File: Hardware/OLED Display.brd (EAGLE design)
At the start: 44.4 x 12.7 mm, 34 parts, among them J1 QWIIC_RIGHT_ANGLE, J3 QWIIC_RIGHT_ANGLE, U2 APX803S-SA, U3 QG-2832TLBFG02

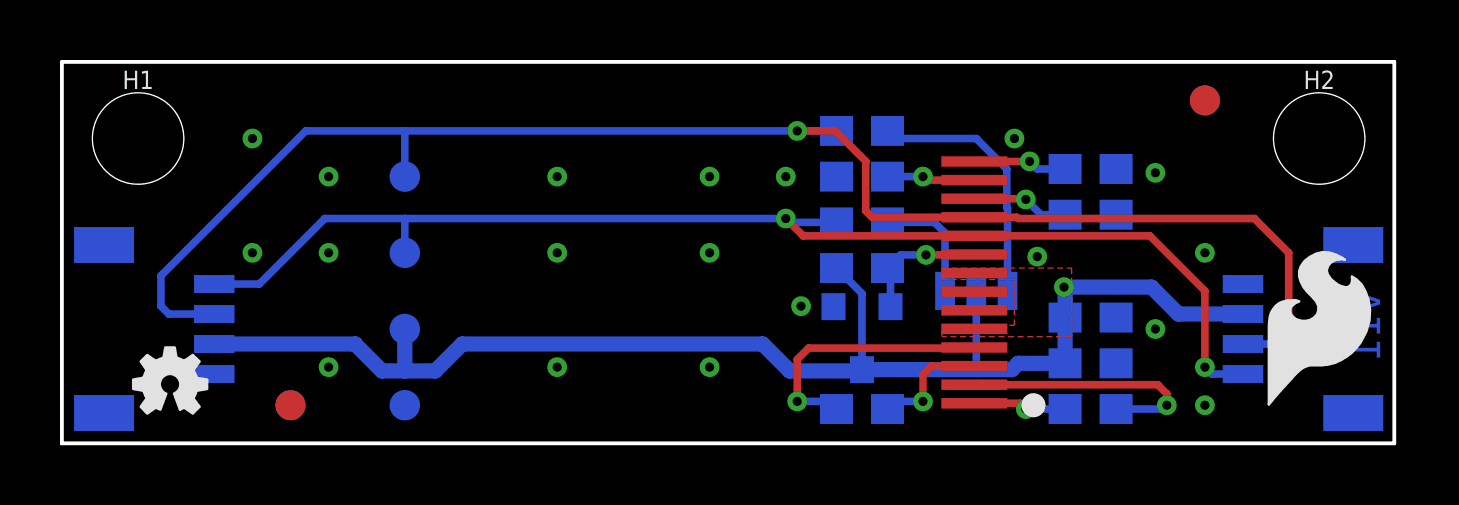
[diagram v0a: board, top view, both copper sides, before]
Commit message: Adds more datasheets, updates part number for OLED display
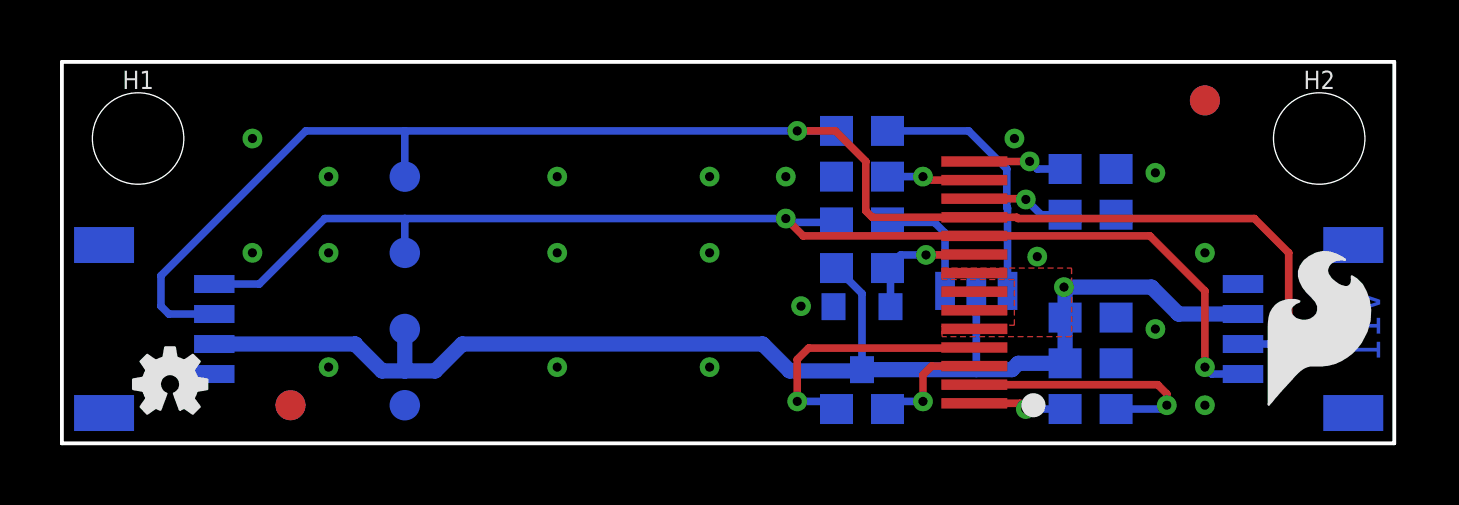
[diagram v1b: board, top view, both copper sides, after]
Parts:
- U3: value QG-2832TLBFG02 -> AMO091-12832BFG02-H14; device Module:QG-2832TLBFG02 -> Module:AMO091-12832BFG02-H14
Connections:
- net RST renamed !RST!
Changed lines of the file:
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@@
 <drawing>
 <settings>
-<setting alwaysvectorfont="yes"/>
+<setting alwaysvectorfont="no"/>
 <setting keepoldvectorfont="yes"/>
 <setting verticaltext="up"/>
@@
 <layer number="45" name="Holes" color="7" fill="1" visible="yes" active="yes"/>
 <layer number="46" name="Milling" color="3" fill="1" visible="no" active="yes"/>
-<layer number="47" name="Measures" color="7" fill="1" visible="yes" active="yes"/>
+<layer number="47" name="Measures" color="7" fill="1" visible="no" active="yes"/>
 <layer number="48" name="Document" color="7" fill="1" visible="no" active="yes"/>
 <layer number="49" name="Reference" color="13" fill="1" visible="yes" active="yes"/>
@@
 <element name="U2" library="Module" package="SOT23-3" value="APX803S-SA" x="26.67" y="3.556" smashed="yes" rot="MR180">
 <attribute name="NAME" x="25.019" y="3.556" size="0.6096" layer="26" font="vector" ratio="20" rot="MR270" align="bottom-center"/>
-<attribute name="PROD_ID" value="" x="26.67" y="3.556" size="1.778" layer="28" font="vector" ratio="15" rot="MR180" display="off"/>
+<attribute name="PROD_ID" value="IC-21146" x="26.67" y="3.556" size="1.778" layer="28" font="vector" ratio="15" rot="MR180" display="off"/>
 <attribute name="VALUE" x="28.321" y="3.556" size="0.6096" layer="28" font="vector" ratio="20" rot="MR270" align="top-center"/>
 </element>
 <element name="LOGO1" library="SparkFun-Aesthetics" package="SFE_LOGO_NAME_FLAME_.1" value="SFE_LOGO_NAME_FLAME.1_INCH" x="17.78" y="7.62" smashed="yes" rot="MR0"/>
 <element name="U$1" library="SparkFun-Aesthetics" package="SFE_LOGO_FLAME_.2" value="" x="41.91" y="3.81" smashed="yes"/>
-<element name="U3" library="Module" package="QG-2832TLBFG02" value="QG-2832TLBFG02" x="30.48" y="5.08" smashed="yes">
+<element name="U3" library="Module" package="AMO091-12832BFG02-H14" value="AMO091-12832BFG02-H14" x="30.48" y="5.08" smashed="yes">
 <attribute name="NAME" x="28.829" y="9.779" size="0.6096" layer="27" font="vector" ratio="20"/>
-<attribute name="PROD_ID" value="" x="30.48" y="5.08" size="1.778" layer="27" font="vector" ratio="15" display="off"/>
+<attribute name="PROD_ID" value="LCD-21145" x="30.48" y="5.08" size="1.778" layer="27" font="vector" ratio="15" display="off"/>
 <attribute name="VALUE" x="28.702" y="0.127" size="0.6096" layer="27" font="vector" ratio="20"/>
 </element>
@@
 <via x="32.512" y="6.223" extent="1-16" drill="0.3048"/>
 <contactref element="TP4" pad="1"/>
+<wire x1="38.1" y1="6.35" x2="39.37" y2="5.31" width="0" layer="19" extent="16-16"/>
+<wire x1="36.449" y1="3.81" x2="38.1" y2="6.35" width="0" layer="19" extent="1-1"/>
+<wire x1="35.14" y1="4.191" x2="36.449" y2="3.81" width="0" layer="19" extent="16-16"/>
+<wire x1="35.14" y1="2.667" x2="35.14" y2="4.191" width="0" layer="19" extent="16-16"/>
+<wire x1="38.1" y1="1.27" x2="36.449" y2="3.81" width="0" layer="19" extent="1-1"/>
+<wire x1="36.449" y1="9.017" x2="38.1" y2="6.35" width="0" layer="19" extent="1-1"/>
+<wire x1="35.14" y1="9.144" x2="36.449" y2="9.017" width="0" layer="19" extent="16-16"/>
+<wire x1="35.14" y1="7.62" x2="35.14" y2="9.144" width="0" layer="19" extent="16-16"/>
+<wire x1="32.512" y1="6.223" x2="35.14" y2="7.62" width="0" layer="19" extent="16-16"/>
+<wire x1="30.414" y1="5.054" x2="32.512" y2="6.223" width="0" layer="19" extent="1-1"/>
+<wire x1="31.75" y1="10.16" x2="35.14" y2="9.144" width="0" layer="19" extent="16-16"/>
+<wire x1="25.72" y1="4.556" x2="30.414" y2="5.054" width="0" layer="19" extent="1-16"/>
+<wire x1="24.638" y1="4.572" x2="25.72" y2="4.556" width="0" layer="19" extent="16-16"/>
+<wire x1="21.59" y1="6.35" x2="24.638" y2="4.572" width="0" layer="19" extent="1-1"/>
+<wire x1="21.59" y1="8.89" x2="21.59" y2="6.35" width="0" layer="19" extent="1-1"/>
+<wire x1="24.13" y1="8.89" x2="21.59" y2="8.89" width="0" layer="19" extent="1-1"/>
+<wire x1="25.82" y1="8.89" x2="24.13" y2="8.89" width="0" layer="19" extent="16-16"/>
+<wire x1="21.59" y1="2.54" x2="24.638" y2="4.572" width="0" layer="19" extent="1-1"/>
+<wire x1="16.51" y1="8.89" x2="21.59" y2="8.89" width="0" layer="19" extent="1-1"/>
+<wire x1="16.51" y1="6.35" x2="16.51" y2="8.89" width="0" layer="19" extent="1-1"/>
+<wire x1="16.51" y1="2.54" x2="16.51" y2="6.35" width="0" layer="19" extent="1-1"/>
+<wire x1="11.43" y1="1.27" x2="16.51" y2="2.54" width="0" layer="19" extent="16-16"/>
+<wire x1="8.89" y1="2.54" x2="11.43" y2="1.27" width="0" layer="19" extent="16-16"/>
+<wire x1="8.89" y1="6.35" x2="8.89" y2="2.54" width="0" layer="19" extent="1-1"/>
+<wire x1="8.89" y1="8.89" x2="8.89" y2="6.35" width="0" layer="19" extent="1-1"/>
+<wire x1="6.35" y1="6.35" x2="8.89" y2="6.35" width="0" layer="19" extent="1-1"/>
+<wire x1="6.35" y1="10.16" x2="8.89" y2="8.89" width="0" layer="19" extent="1-1"/>
+<wire x1="5.08" y1="2.31" x2="8.89" y2="2.54" width="0" layer="19" extent="16-16"/>
 </signal>
 <signal name="SCL">
@@
 <wire x1="32.254" y1="9.394" x2="30.414" y2="9.394" width="0.254" layer="1"/>
 </signal>
-<signal name="RST">
+<signal name="!RST!">
 <contactref element="R4" pad="1"/>
 <contactref element="U2" pad="2"/>
@@
 <contactref element="R2" pad="2"/>
 <contactref element="I2C" pad="1"/>
-<wire x1="27.94" y1="10.16" x2="27.686" y2="10.414" width="0.254" layer="16"/>
-<wire x1="27.686" y1="10.414" x2="27.52" y2="10.414" width="0.254" layer="16"/>
+<wire x1="31.496" y1="9.144" x2="30.226" y2="10.414" width="0.254" layer="16"/>
+<wire x1="30.226" y1="10.414" x2="27.52" y2="10.414" width="0.254" layer="16"/>
 <wire x1="31.5214" y1="5.08" x2="31.5214" y2="7.83956875" width="0.254" layer="16"/>
 <wire x1="31.5214" y1="7.83956875" x2="31.496" y2="7.86496875" width="0.254" layer="16"/>
 <wire x1="31.496" y1="7.86496875" x2="31.496" y2="9.144" width="0.254" layer="16"/>
-<wire x1="30.48" y1="10.16" x2="27.94" y2="10.16" width="0.254" layer="16"/>
-<wire x1="31.496" y1="9.144" x2="30.48" y2="10.16" width="0.254" layer="16"/>
 </signal>
 <signal name="3.3V">

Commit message: Adds more measures
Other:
- board text added: "1.6mm Thickness 1 oz. Copper Lead-Free HASL finish Material: TG135-140 Red Soldermask White Silkscreen Two Layer"
- board text removed: "1.6mm Thickness 1 oz. Copper Lead-Free HASL finish Material: TG135-140 Red Soldermask White Silkscreen"
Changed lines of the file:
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@@
 <setting verticaltext="up"/>
 </settings>
-<grid distance="0.05" unitdist="inch" unit="inch" style="dots" multiple="1" display="yes" altdistance="0.005" altunitdist="inch" altunit="inch"/>
+<grid distance="0.05" unitdist="inch" unit="inch" style="dots" multiple="1" display="yes" altdistance="0.002" altunitdist="inch" altunit="inch"/>
 <layers>
 <layer number="1" name="Top" color="4" fill="1" visible="yes" active="yes"/>
@@
 <layer number="45" name="Holes" color="7" fill="1" visible="yes" active="yes"/>
 <layer number="46" name="Milling" color="3" fill="1" visible="no" active="yes"/>
-<layer number="47" name="Measures" color="7" fill="1" visible="no" active="yes"/>
+<layer number="47" name="Measures" color="7" fill="1" visible="yes" active="yes"/>
 <layer number="48" name="Document" color="7" fill="1" visible="no" active="yes"/>
 <layer number="49" name="Reference" color="13" fill="1" visible="yes" active="yes"/>
@@
 <text x="31.75" y="-14.478" size="1.778" layer="51" font="vector">NOA Labs</text>
 <text x="12.7" y="-17.78" size="1.778" layer="51" font="vector">Revised By: Elias Santistevan</text>
-<dimension x1="44.4246" y1="12.7" x2="0" y2="12.7" x3="22.2123" y3="19.05" textsize="1.778" textratio="15" layer="47" unit="inch"/>
+<dimension x1="44.4246" y1="12.7" x2="0" y2="12.7" x3="22.2123" y3="24.13" textsize="1.778" textratio="15" layer="47" unit="inch"/>
 <dimension x1="41.91" y1="10.16" x2="44.45" y2="10.16" x3="43.18" y3="13.97" textsize="1.778" textratio="15" layer="47" unit="inch"/>
 <dimension x1="0" y1="12.7" x2="0" y2="0" x3="-12.7" y3="6.35" textsize="1.778" textratio="15" layer="47" unit="inch"/>
@@
 <dimension x1="41.91" y1="3.81" x2="41.91" y2="0" x3="49.53" y3="1.905" textsize="1.778" textratio="15" layer="47" unit="inch"/>
 <text x="11.43" y="-5.08" size="1.778" layer="47" font="vector" ratio="15">Units in Inches</text>
-<text x="59.69" y="25.4" size="1.778" layer="51" font="vector">1.6mm Thickness
+<text x="59.69" y="22.86" size="1.778" layer="51" font="vector">1.6mm Thickness
 1 oz. Copper
 Lead-Free HASL finish
 Material: TG135-140
 Red Soldermask
-White Silkscreen</text>
+White Silkscreen
+Two Layer</text>
 <text x="43.942" y="5.08" size="1.016" layer="16" font="vector" ratio="20" rot="SMR270">v11</text>
+<dimension x1="0" y1="12.7" x2="5.969" y2="11.176" x3="2.9845" y3="15.24" textsize="1.778" textratio="15" layer="47" dtype="horizontal" unit="inch"/>
+<dimension x1="0" y1="12.7" x2="38.5572" y2="12.0904" x3="19.2786" y3="19.05" textsize="1.778" textratio="15" layer="47" dtype="horizontal" unit="inch"/>
 </plain>
 <attributes>
@@
 <via x="32.512" y="6.223" extent="1-16" drill="0.3048"/>
 <contactref element="TP4" pad="1"/>
-<wire x1="38.1" y1="6.35" x2="39.37" y2="5.31" width="0" layer="19" extent="16-16"/>
-<wire x1="36.449" y1="3.81" x2="38.1" y2="6.35" width="0" layer="19" extent="1-1"/>
-<wire x1="35.14" y1="4.191" x2="36.449" y2="3.81" width="0" layer="19" extent="16-16"/>
-<wire x1="35.14" y1="2.667" x2="35.14" y2="4.191" width="0" layer="19" extent="16-16"/>
-<wire x1="38.1" y1="1.27" x2="36.449" y2="3.81" width="0" layer="19" extent="1-1"/>
-<wire x1="36.449" y1="9.017" x2="38.1" y2="6.35" width="0" layer="19" extent="1-1"/>
-<wire x1="35.14" y1="9.144" x2="36.449" y2="9.017" width="0" layer="19" extent="16-16"/>
-<wire x1="35.14" y1="7.62" x2="35.14" y2="9.144" width="0" layer="19" extent="16-16"/>
-<wire x1="32.512" y1="6.223" x2="35.14" y2="7.62" width="0" layer="19" extent="16-16"/>
-<wire x1="30.414" y1="5.054" x2="32.512" y2="6.223" width="0" layer="19" extent="1-1"/>
-<wire x1="31.75" y1="10.16" x2="35.14" y2="9.144" width="0" layer="19" extent="16-16"/>
-<wire x1="25.72" y1="4.556" x2="30.414" y2="5.054" width="0" layer="19" extent="1-16"/>
-<wire x1="24.638" y1="4.572" x2="25.72" y2="4.556" width="0" layer="19" extent="16-16"/>
-<wire x1="21.59" y1="6.35" x2="24.638" y2="4.572" width="0" layer="19" extent="1-1"/>
-<wire x1="21.59" y1="8.89" x2="21.59" y2="6.35" width="0" layer="19" extent="1-1"/>
-<wire x1="24.13" y1="8.89" x2="21.59" y2="8.89" width="0" layer="19" extent="1-1"/>
-<wire x1="25.82" y1="8.89" x2="24.13" y2="8.89" width="0" layer="19" extent="16-16"/>
-<wire x1="21.59" y1="2.54" x2="24.638" y2="4.572" width="0" layer="19" extent="1-1"/>
-<wire x1="16.51" y1="8.89" x2="21.59" y2="8.89" width="0" layer="19" extent="1-1"/>
-<wire x1="16.51" y1="6.35" x2="16.51" y2="8.89" width="0" layer="19" extent="1-1"/>
-<wire x1="16.51" y1="2.54" x2="16.51" y2="6.35" width="0" layer="19" extent="1-1"/>
-<wire x1="11.43" y1="1.27" x2="16.51" y2="2.54" width="0" layer="19" extent="16-16"/>
-<wire x1="8.89" y1="2.54" x2="11.43" y2="1.27" width="0" layer="19" extent="16-16"/>
-<wire x1="8.89" y1="6.35" x2="8.89" y2="2.54" width="0" layer="19" extent="1-1"/>
-<wire x1="8.89" y1="8.89" x2="8.89" y2="6.35" width="0" layer="19" extent="1-1"/>
-<wire x1="6.35" y1="6.35" x2="8.89" y2="6.35" width="0" layer="19" extent="1-1"/>
-<wire x1="6.35" y1="10.16" x2="8.89" y2="8.89" width="0" layer="19" extent="1-1"/>
-<wire x1="5.08" y1="2.31" x2="8.89" y2="2.54" width="0" layer="19" extent="16-16"/>
 </signal>
 <signal name="SCL">
@@
 <vertex x="29.337" y="3.556"/>
 </polygon>
-<wire x1="33.397" y1="2.71" x2="33.44" y2="2.667" width="0.508" layer="16"/>
 <wire x1="33.44" y1="2.667" x2="33.44" y2="4.191" width="0.508" layer="16"/>
 <wire x1="33.44" y1="5.168" x2="33.401" y2="5.207" width="0.508" layer="16"/>
@@
 <wire x1="12.446" y1="2.413" x2="13.343" y2="3.31" width="0.508" layer="16"/>
 <wire x1="11.43" y1="3.81" x2="11.43" y2="2.413" width="0.508" layer="16"/>
-<wire x1="30.48" y1="5.08" x2="30.414" y2="5.674" width="0" layer="19" extent="1-16"/>
-<wire x1="30.414" y1="3.814" x2="30.48" y2="5.08" width="0" layer="19" extent="1-16"/>
 </signal>
 <signal name="N$1">

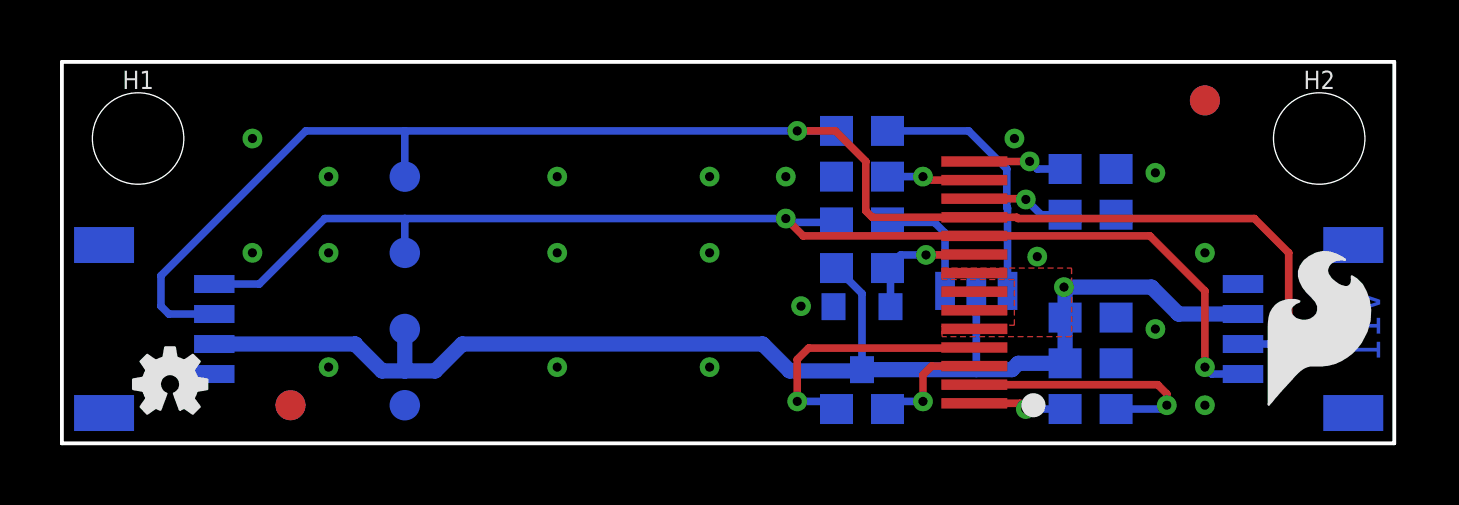
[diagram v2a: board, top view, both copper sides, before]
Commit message: Swaps right angle Qwiic connector to vertical
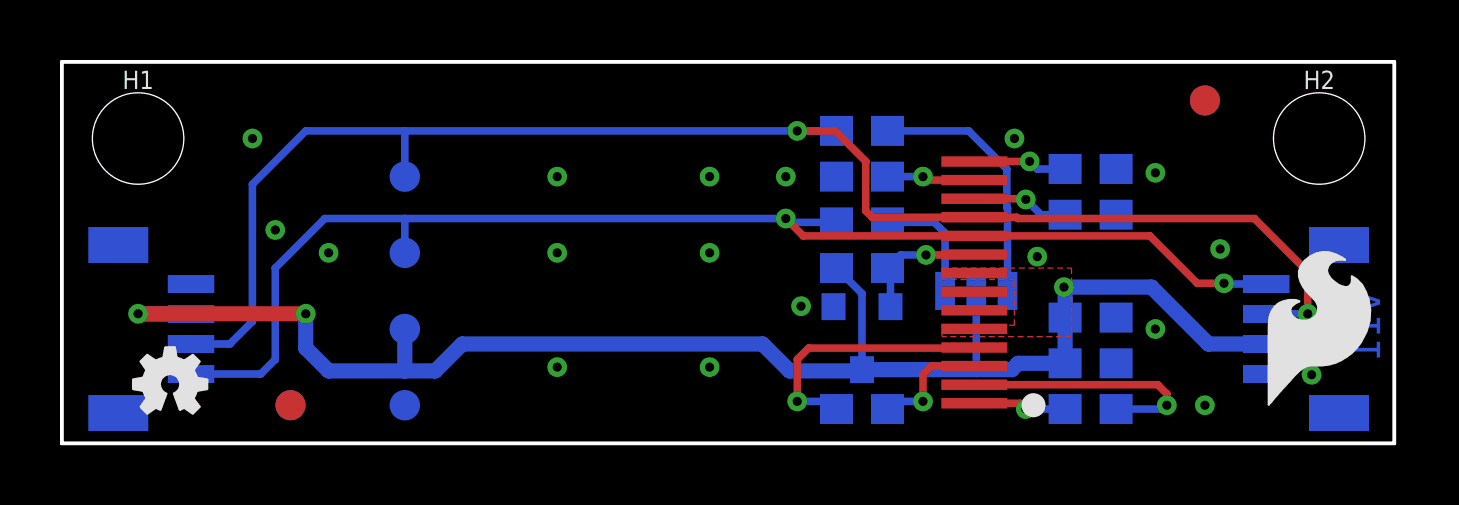
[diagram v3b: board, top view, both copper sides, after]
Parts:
- J1, J3: value QWIIC_RIGHT_ANGLE -> Vertical Qwiic Connector; device SparkFun-Connectors:JST04_1MM_RA -> SparkFun-Connectors:JST04_1MM_VERT
- turned J1 to 90 degrees
- turned J3 to 270 degrees
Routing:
- net 3.3V: track 46.2 -> 52.8 mm, vias 1 -> 3
- net SCL: track 41.7 -> 43.6 mm
- net SDA: track 52.3 -> 51.4 mm
